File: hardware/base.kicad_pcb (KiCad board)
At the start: 4 copper layers, 100 x 85 mm, 304 parts, among them J101 USB-A, J102 TNG-Data-TOP, J103 TNG-Power-TOP, J301 MICROSDCARD, J302 Raspberry-Pi-Compute-Socket, J303 MICRO_HDMI, J304 USB Micro, J401 RJSLG-001TA1, P101 Debug, P102 Boot, P103 PE, P201 DI IN, P202 PWR IN, P301 XMC Flash, Q301 2N7002P, Q302 2N7002P, Q303 2N7002P, Q304 2N7002P, Q305 2N7002P, T201 744272251, U101 USB2517, U102 MIC2026-1YM, U103 82400152, U104 XMC1XXX24, U105 TPD4S010DQA, U106 TPD4S010DQA, U107 TPD4S010DQA, U108 AP7333-33SAG-7, U109 TPS22975, U110 TPS22975, U111 PCT2075DP, U112 VN7140AS, U201 ISO1211, U202 FPF2700MX, U203 BD90640HFP, U204 PAC1933, U301 PAM2306AYPAA, U302 PCF8523T, U303 FSUSB42MUX, U304 TPD4S010DQA, U305 TPD4S010DQA, U306 TPD4S010DQA, U307 82400152, U308 ATECC608A, U309 AP2331, U310 SLB9670, U401 LAN7500, U402 93AA66, U403 TPD4S010DQA, U404 TPD4S010DQA, U405 PAM2306AYPAA, X101 24MHz, X301 32.768kHz, X401 25MHz

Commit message: add testpoints for power supplies, flash interface
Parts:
- added P104: TST_GND, kicad-libraries:TSTPT, B.Cu at (121.0, 80.8)
- added P105: TST_3V3P, kicad-libraries:TSTPT, B.Cu at (119.0, 83.2)
- added P203: TST_5V, kicad-libraries:TSTPT, B.Cu at (103.5, 96.7)
- added P204: TST_GND, kicad-libraries:TSTPT, B.Cu at (105.5, 98.7)
- added P302: TST_SCL, kicad-libraries:TSTPT, B.Cu at (155.3, 89.0)
- added P303: TST_SDA, kicad-libraries:TSTPT, B.Cu at (155.3, 91.0)
- added P304: TST_WP, kicad-libraries:TSTPT, B.Cu at (155.3, 93.0)
- added P305: TST_3V3, kicad-libraries:TSTPT, B.Cu at (96.5, 74.2)
- added P306: TST_1V8, kicad-libraries:TSTPT, B.Cu at (135.8, 90.3)
- added P307: TST_XMC_11, kicad-libraries:TSTPT, B.Cu at (134.6, 96.9)
- added P401: TST_1V2, kicad-libraries:TSTPT, B.Cu at (102.2, 88.4)
- added R305: 10k, R0402F, B.Cu at (153.2, 92.5)
- P101: moved to B.Cu
- P301: value XMC Flash -> TST_XMC_10; footprint kicad-libraries:PIN_ARRAY_2X1_SMD -> kicad-libraries:TSTPT
- U308: value ATECC608A -> M24256-DFMN6TP
- moved P101 7.50 mm to (122.5, 80.8)
- moved P301 1.45 mm to (134.6, 99.5), turned to 0 degrees
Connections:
- P301 pad 1: Net-(J302-Pad35) -> Net-(J302-Pad33)
- U308 pad 1: Net-(U308-Pad1) -> AGND
- U308 pad 2: Net-(U308-Pad2) -> AGND
- U308 pad 3: Net-(U308-Pad3) -> AGND
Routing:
- net Net-(P101-Pad1): track 12.9 -> 5.38 mm, vias 0 -> 1
- net AGND: track 1107.5 -> 1113.8 mm, vias 589 -> 593
- net Net-(P304-Pad1): track 0.00 -> 4.22 mm
- net Net-(J302-Pad84): track 32.5 -> 36.4 mm
- net 3V3: track 501.0 -> 504.8 mm
- net +5V: track 74.4 -> 77.0 mm, vias 0 -> 1
- net +1.2V: track 73.7 -> 75.7 mm
- net 3V3_PERM: track 225.6 -> 227.0 mm
- net Net-(J302-Pad82): track 34.4 -> 35.7 mm
- net +1.8V: track 123.0 -> 124.2 mm
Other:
- board text added: "Testpunkte für Spannungen + GND auf Unterseite Beschriftungen? Flash Testpunkt ok? TPM? SLB9670VQ20FW785XTMA1? SPI 2 Todo Check Debug auf Unterseite als 0402 (DBG + GND)"
- board text removed: "Flash 1 2"
- board text removed: "Testpunkte für Spannungen + GND auf Unterseite ATECC -> EEPROM + WP (nach außen), Pogo Con dafür mit WP nach außen TPM? SLB9670VQ20FW785XTMA1? SPI 2 Debug auf Unterseite als 0402 (DBG + GND)"

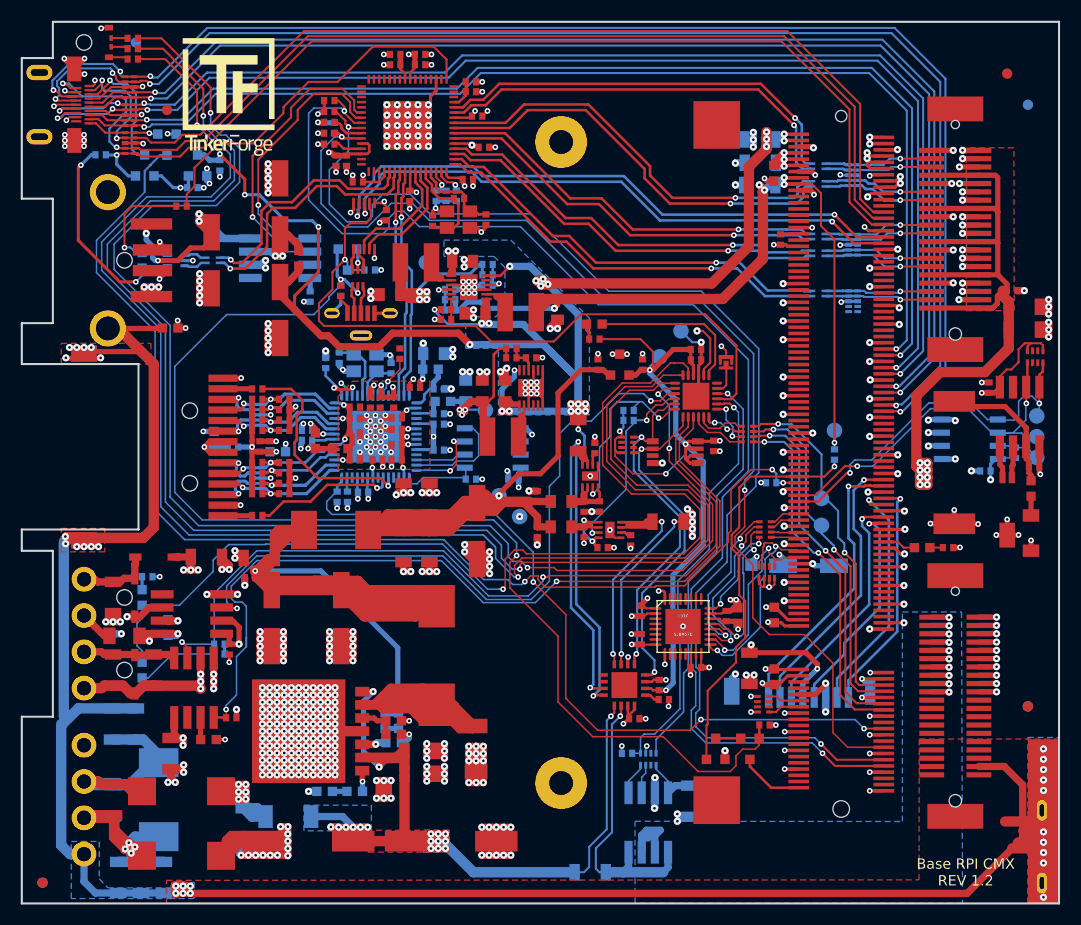
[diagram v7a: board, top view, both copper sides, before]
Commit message: ordered version 1.2
add testpoints
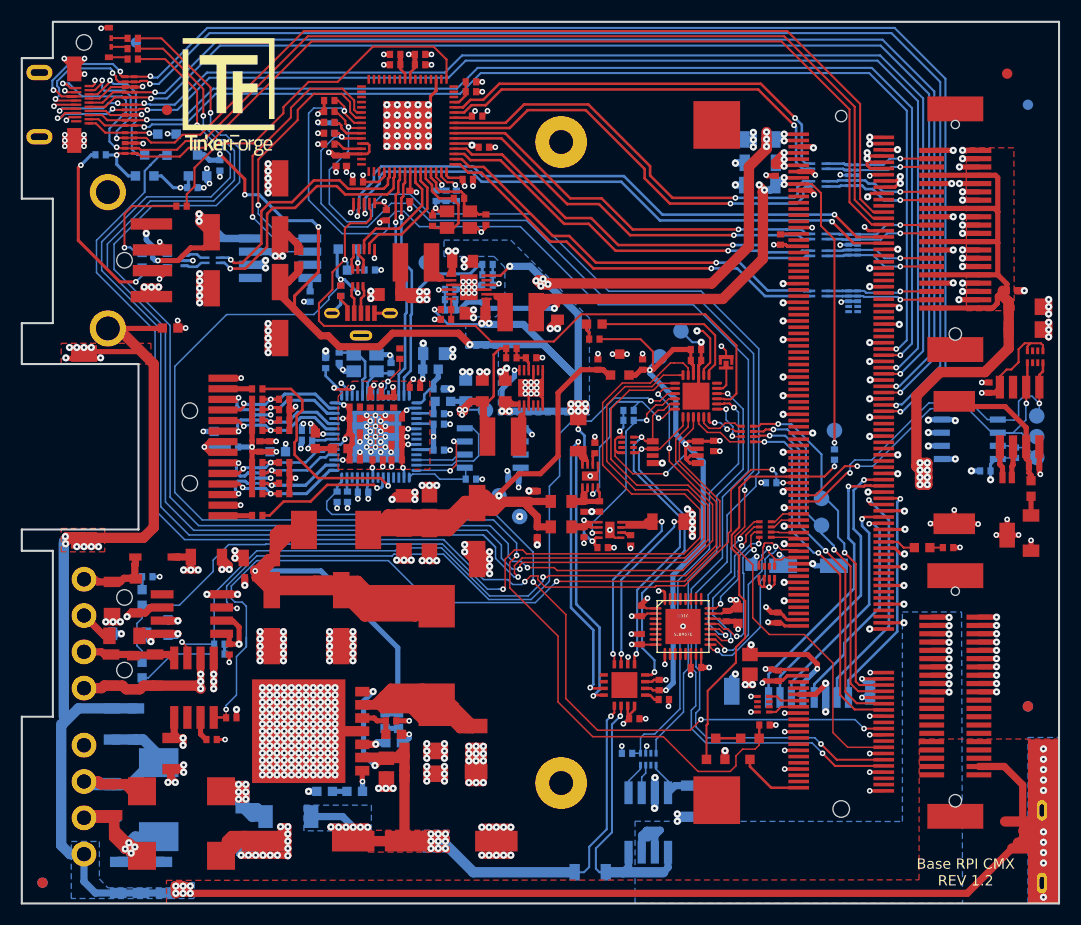
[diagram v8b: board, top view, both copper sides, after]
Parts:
- C101, C102: value 33pF -> 30pF
- C205, C218, C223, C224, C225, C304: footprint C1206 -> kicad-libraries:C0805E
- C208, C307, C308, C310: footprint C0603F -> kicad-libraries:C0402F
- D202, D204, D209: footprint kicad-libraries:SOD-123 -> kicad-libraries:SOD-123FL
- R211: footprint kicad-libraries:R0603F -> kicad-libraries:R0402F
- X401: value 25MHz -> 25MHz_18pF
- moved C121 1.06 mm to (122.5, 83.6)
- moved C122 0.99 mm to (122.5, 82.5)
- moved C224 0.65 mm to (94.3, 100.9)
- moved C218 0.65 mm to (96.8, 97.6)
- moved C225 0.65 mm to (94.2, 97.6)
- moved C223 0.60 mm to (96.8, 101.0)
- moved C205 0.60 mm to (92.6, 122.9)
- moved C310 0.43 mm to (130.3, 108.4)
- moved C307 0.41 mm to (130.4, 114.0)
- moved C304 0.38 mm to (127.7, 112.9)
- moved R211 0.30 mm to (75.8, 120.2)
- moved C308 0.29 mm to (130.1, 65.3)
- moved C208 0.25 mm to (93.0, 118.3)
- moved D204 0.21 mm to (68.2, 113.7), turned to 90 degrees
- moved R202 0.20 mm to (66.0, 113.5)
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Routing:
- net 3V3: track 504.8 -> 505.7 mm
- net AGND: track 1113.8 -> 1114.5 mm, vias 593 -> 591
- net EECS: track 7.44 -> 6.93 mm
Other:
- board text added: "1V2"
- board text added: "1V8"
- board text added: "3V3"
- board text added: "3V3P"
- board text added: "5V"
- board text added: "G10"
- board text added: "G11"
- board text added: "SCL SDA WP"
- board text removed: "Testpunkte für Spannungen + GND auf Unterseite Beschriftungen? Flash Testpunkt ok? TPM? SLB9670VQ20FW785XTMA1? SPI 2 Todo Check Debug auf Unterseite als 0402 (DBG + GND)"
- board text removed: "USB C?"
